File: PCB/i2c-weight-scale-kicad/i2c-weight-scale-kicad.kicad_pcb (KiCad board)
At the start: 2 copper layers, 43 x 49 mm, 13 parts, among them J1 I2C_RJ14, P1 4_STRAIN_GAUGES, U1 INA126, U2 PIC12F1822

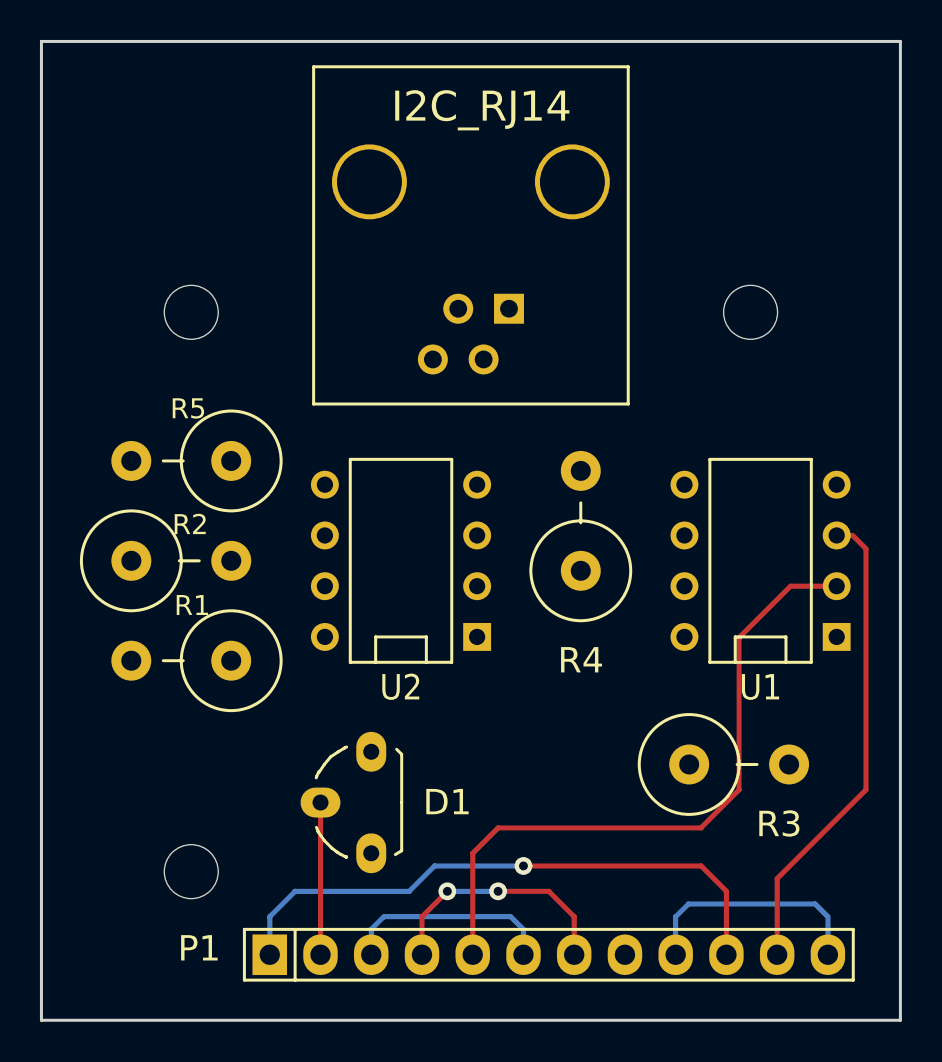
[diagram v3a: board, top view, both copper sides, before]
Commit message: Connect all nets and GND copper fill top and bottom
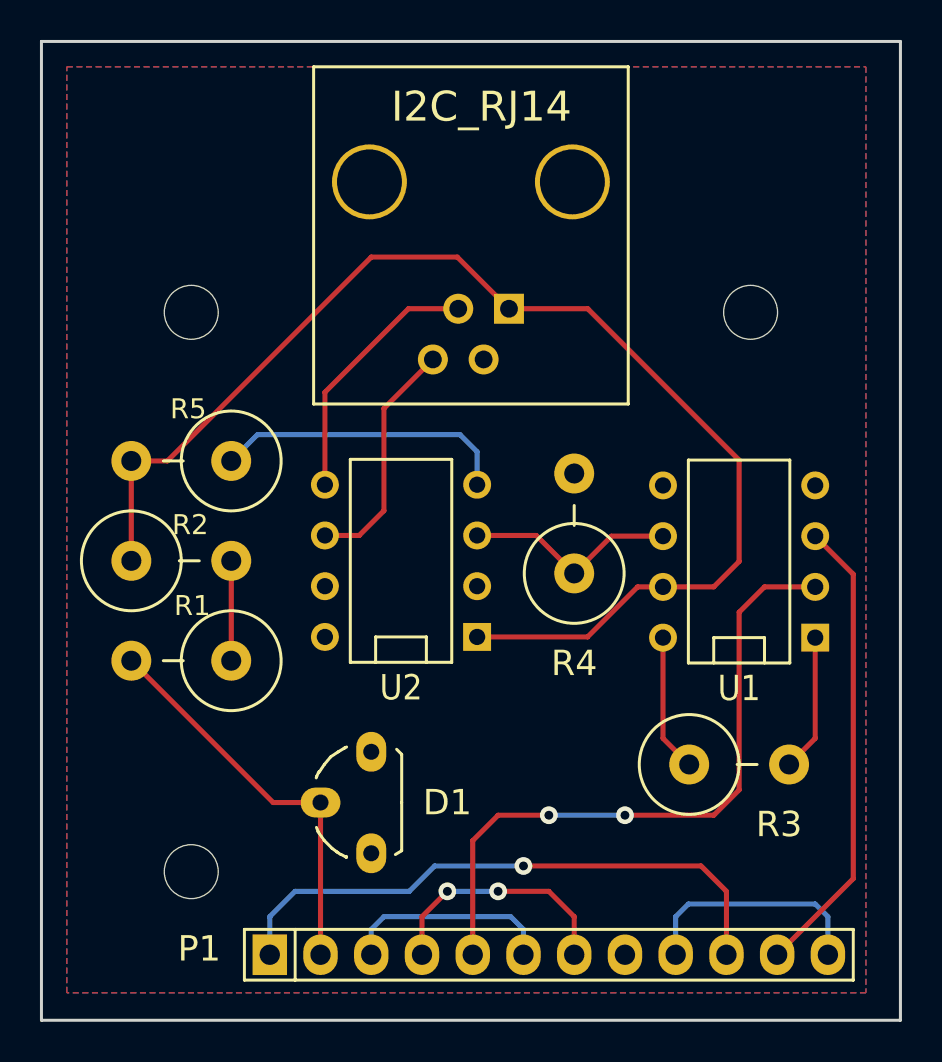
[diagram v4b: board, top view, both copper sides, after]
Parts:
- moved U1 1.08 mm to (84.9, 76.0)
- moved R4 0.35 mm to (76.7, 74.1)
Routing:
- net VDD: track 0.00 -> 63.6 mm
- net Net-(R5-Pad1): track 0.00 -> 14.9 mm
- net Net-(J1-Pad3): track 0.00 -> 13.0 mm
- net Net-(D1-Pad2): track 7.62 -> 20.0 mm
- net Net-(J1-Pad4): track 0.00 -> 12.1 mm
- net Net-(R4-Pad1): track 0.00 -> 10.9 mm
- net Net-(R3-Pad1): track 0.00 -> 6.89 mm
- net Net-(R3-Pad2): track 0.00 -> 6.89 mm
- net Net-(R1-Pad1): track 0.00 -> 5.00 mm
- net Net-(P1-Pad11): track 23.9 -> 23.3 mm
- net Net-(P1-Pad5): vias 0 -> 2
- added copper zone on B.Cu, net GND
- added copper zone on F.Cu, net GND

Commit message: Remove mechanical holes
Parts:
- removed MH (x3): MountingHole_2-7mm_RevA_Date21Jun2010, Mounting_Holes:MountingHole_2-7mm

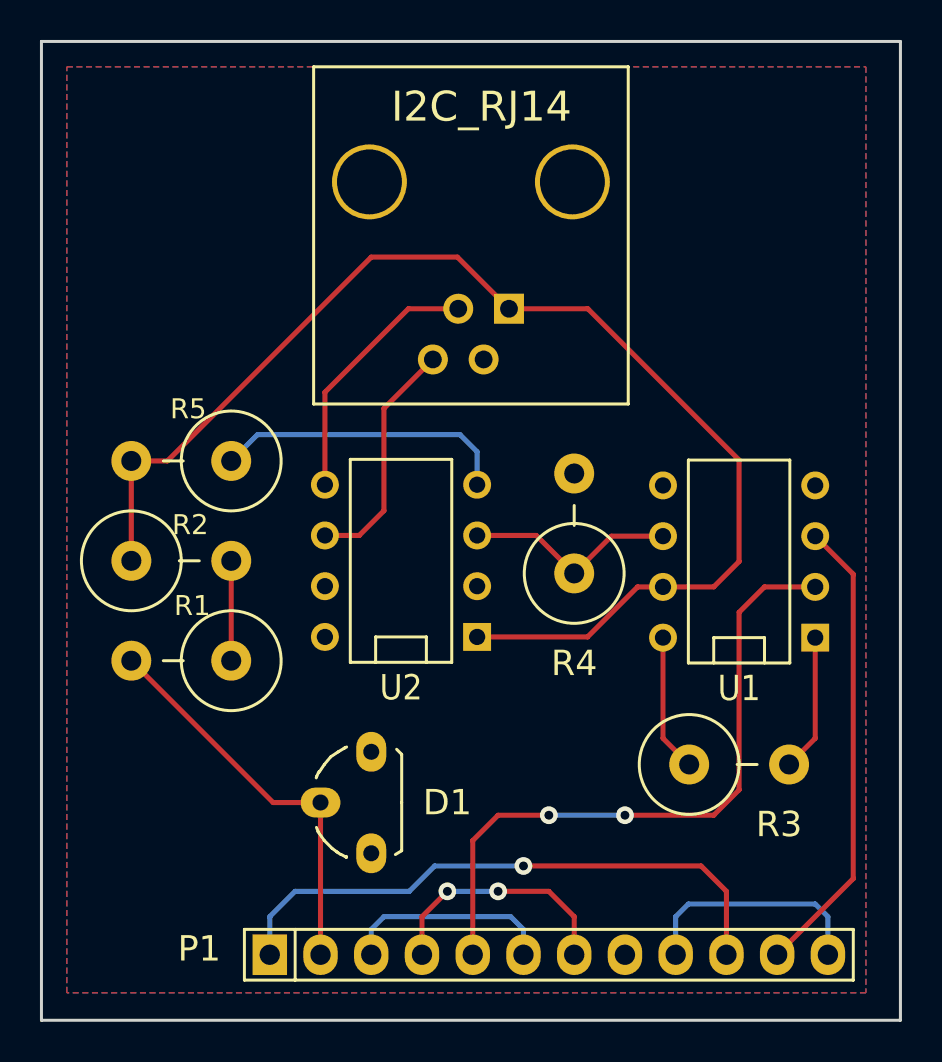
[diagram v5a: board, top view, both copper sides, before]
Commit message: Create new mounting holes
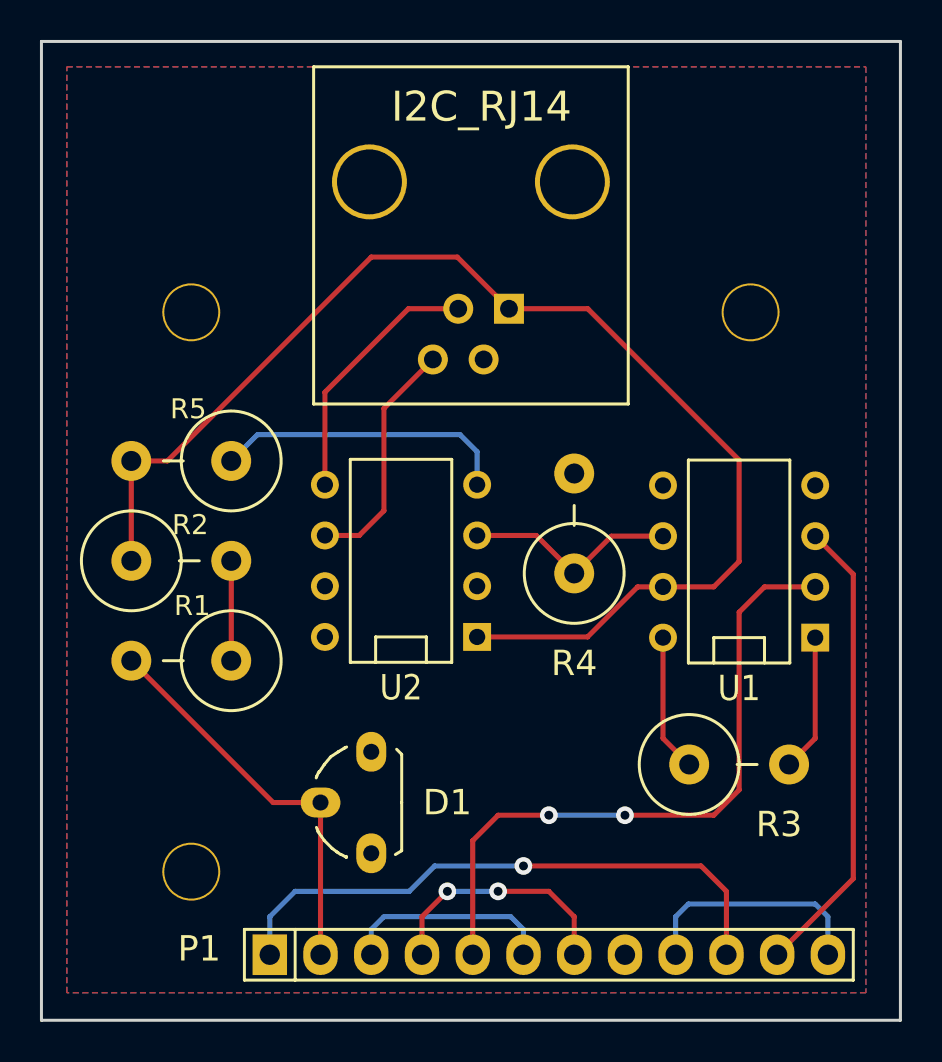
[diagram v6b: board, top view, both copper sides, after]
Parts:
- added MountingHole_2-7mm: VAL**, Mounting_Holes:MountingHole_2-7mm, F.Cu at (57.5, 63.6)
- added MountingHole_2-7mm: VAL**, Mounting_Holes:MountingHole_2-7mm, F.Cu at (85.5, 63.6)
- added MountingHole_2-7mm: VAL**, Mounting_Holes:MountingHole_2-7mm, F.Cu at (57.5, 91.6)
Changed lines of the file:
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@@
   (general
     (links 26)
-    (no_connects 6)
-    (area 31.86523 49.924999 111.33289 99.075001)
+    (no_connects 0)
+    (area 48.361476 49.924999 93.075001 99.075001)
     (thickness 1.6)
     (drawings 4)
     (tracks 79)
     (zones 0)
-    (modules 10)
+    (modules 13)
     (nets 20)
   )
@@
     (mod_text_size 1.5 1.5)
     (mod_text_width 0.15)
-    (pad_size 1.5 1.5)
-    (pad_drill 0.89)
+    (pad_size 2.9 2.9)
+    (pad_drill 2.7)
     (pad_to_mask_clearance 0.2)
     (aux_axis_origin 50 50)
@@
       (net 6 VDD))
   )
+  (module Mounting_Holes:MountingHole_2-7mm (layer F.Cu)
+    (at 57.5 63.56)
+    (descr "Mounting hole, Befestigungsbohrung, 2,7mm, No Annular, Kein Restring,")
+    (tags "Mounting hole, Befestigungsbohrung, 2,7mm, No Annular, Kein Restring,")
+    (fp_text reference MountingHole_2-7mm (at 0 -4.0005) (layer F.SilkS) hide
+      (effects (font (size 1 1) (thickness 0.15)))
+    )
+    (fp_text value VAL** (at 0.09906 3.59918) (layer F.SilkS) hide
+      (effects (font (size 1 1) (thickness 0.15)))
+    )
+    (fp_circle (center 0 0) (end 2.70002 0) (layer Cmts.User) (width 0.381))
+    (pad "" np_thru_hole circle (at 0 0) (size 2.9 2.9) (drill 2.7) (layers *.Cu *.SilkS *.Mask))
+  )
+  (module Mounting_Holes:MountingHole_2-7mm (layer F.Cu)
+    (at 85.5 63.56)
+    (descr "Mounting hole, Befestigungsbohrung, 2,7mm, No Annular, Kein Restring,")
+    (tags "Mounting hole, Befestigungsbohrung, 2,7mm, No Annular, Kein Restring,")
+    (fp_text reference MountingHole_2-7mm (at 0 -4.0005) (layer F.SilkS) hide
+      (effects (font (size 1 1) (thickness 0.15)))
+    )
+    (fp_text value VAL** (at 0.09906 3.59918) (layer F.SilkS) hide
+      (effects (font (size 1 1) (thickness 0.15)))
+    )
+    (fp_circle (center 0 0) (end 2.70002 0) (layer Cmts.User) (width 0.381))
+    (pad "" np_thru_hole circle (at 0 0) (size 2.9 2.9) (drill 2.7) (layers *.Cu *.SilkS *.Mask))
+  )
+  (module Mounting_Holes:MountingHole_2-7mm (layer F.Cu)
+    (at 57.5 91.56)
+    (descr "Mounting hole, Befestigungsbohrung, 2,7mm, No Annular, Kein Restring,")
+    (tags "Mounting hole, Befestigungsbohrung, 2,7mm, No Annular, Kein Restring,")
+    (fp_text reference MountingHole_2-7mm (at 0 -4.0005) (layer F.SilkS) hide
+      (effects (font (size 1 1) (thickness 0.15)))
+    )
+    (fp_text value VAL** (at 0.09906 3.59918) (layer F.SilkS) hide
+      (effects (font (size 1 1) (thickness 0.15)))
+    )
+    (fp_circle (center 0 0) (end 2.70002 0) (layer Cmts.User) (width 0.381))
+    (pad "" np_thru_hole circle (at 0 0) (size 2.9 2.9) (drill 2.7) (layers *.Cu *.SilkS *.Mask))
+  )
   (gr_line (start 50 99) (end 50 50) (angle 90) (layer Edge.Cuts) (width 0.15))

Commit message: Add text
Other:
- board text added: "I2C Weight Scale"
- board text added: "Rev 0.1.0 By simlun"
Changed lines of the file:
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@@
     (links 26)
     (no_connects 0)
-    (area 48.361476 49.924999 93.075001 99.075001)
+    (area 48.861476 49.924999 94.138524 99.075001)
     (thickness 1.6)
-    (drawings 4)
+    (drawings 6)
     (tracks 79)
     (zones 0)
@@
   (layers
     (0 F.Cu signal)
-    (31 B.Cu signal)
+    (31 B.Cu signal hide)
     (32 B.Adhes user)
     (33 F.Adhes user)
@@
     (visible_elements FFFFFF7F)
     (pcbplotparams
-      (layerselection 0x00030_80000001)
+      (layerselection 0x010f0_80000001)
       (usegerberextensions false)
       (excludeedgelayer true)
@@
       (outputformat 1)
       (mirror false)
-      (drillshape 1)
+      (drillshape 0)
       (scaleselection 1)
-      (outputdirectory ""))
+      (outputdirectory Gerbers/))
   )
   (net 0 "")
@@
     (pad "" np_thru_hole circle (at 0 0) (size 2.9 2.9) (drill 2.7) (layers *.Cu *.SilkS *.Mask))
   )
+  (gr_text "Rev 0.1.0\nBy simlun" (at 81.17 53.94) (layer F.SilkS)
+    (effects (font (size 1.2 1.2) (thickness 0.2)) (justify left))
+  )
+  (gr_text "I2C\nWeight\nScale" (at 55.54 55.54) (layer F.Cu)
+    (effects (font (size 1.5 1.5) (thickness 0.3)))
+  )
   (gr_line (start 50 99) (end 50 50) (angle 90) (layer Edge.Cuts) (width 0.15))
